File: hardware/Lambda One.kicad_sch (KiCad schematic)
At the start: 23 parts, among them IC1 DS1818, SW1 SW_Push, U8 74HC00, U9 74HC00, Y1 TFT680

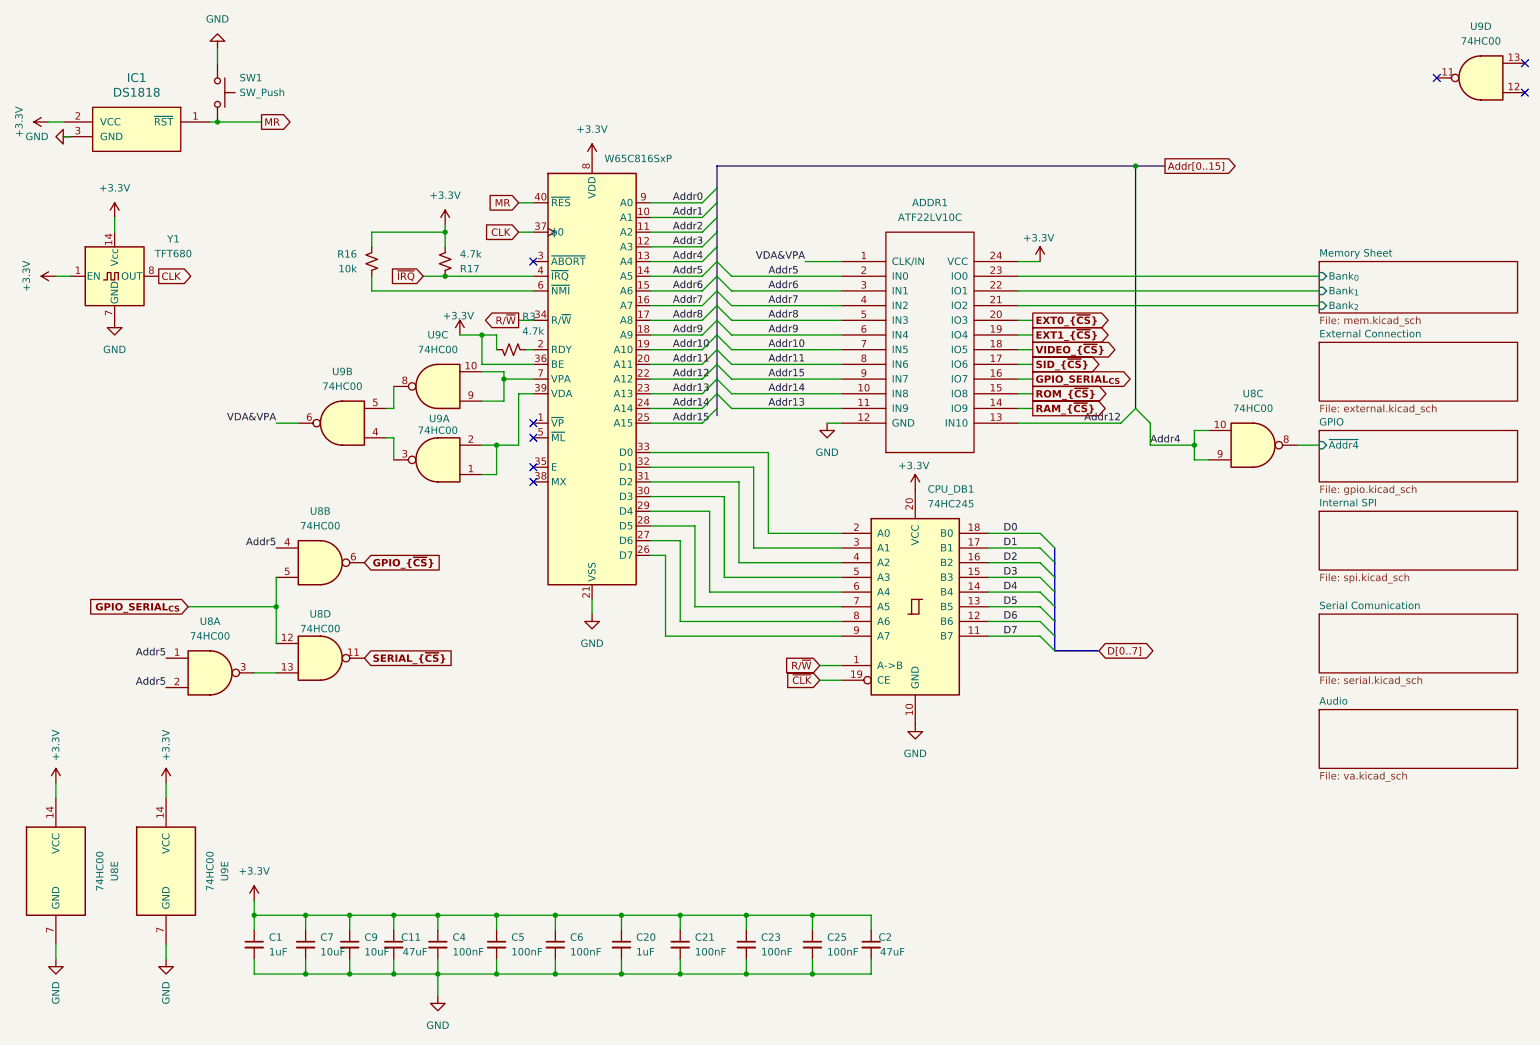
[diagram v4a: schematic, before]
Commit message: Removed old VPU
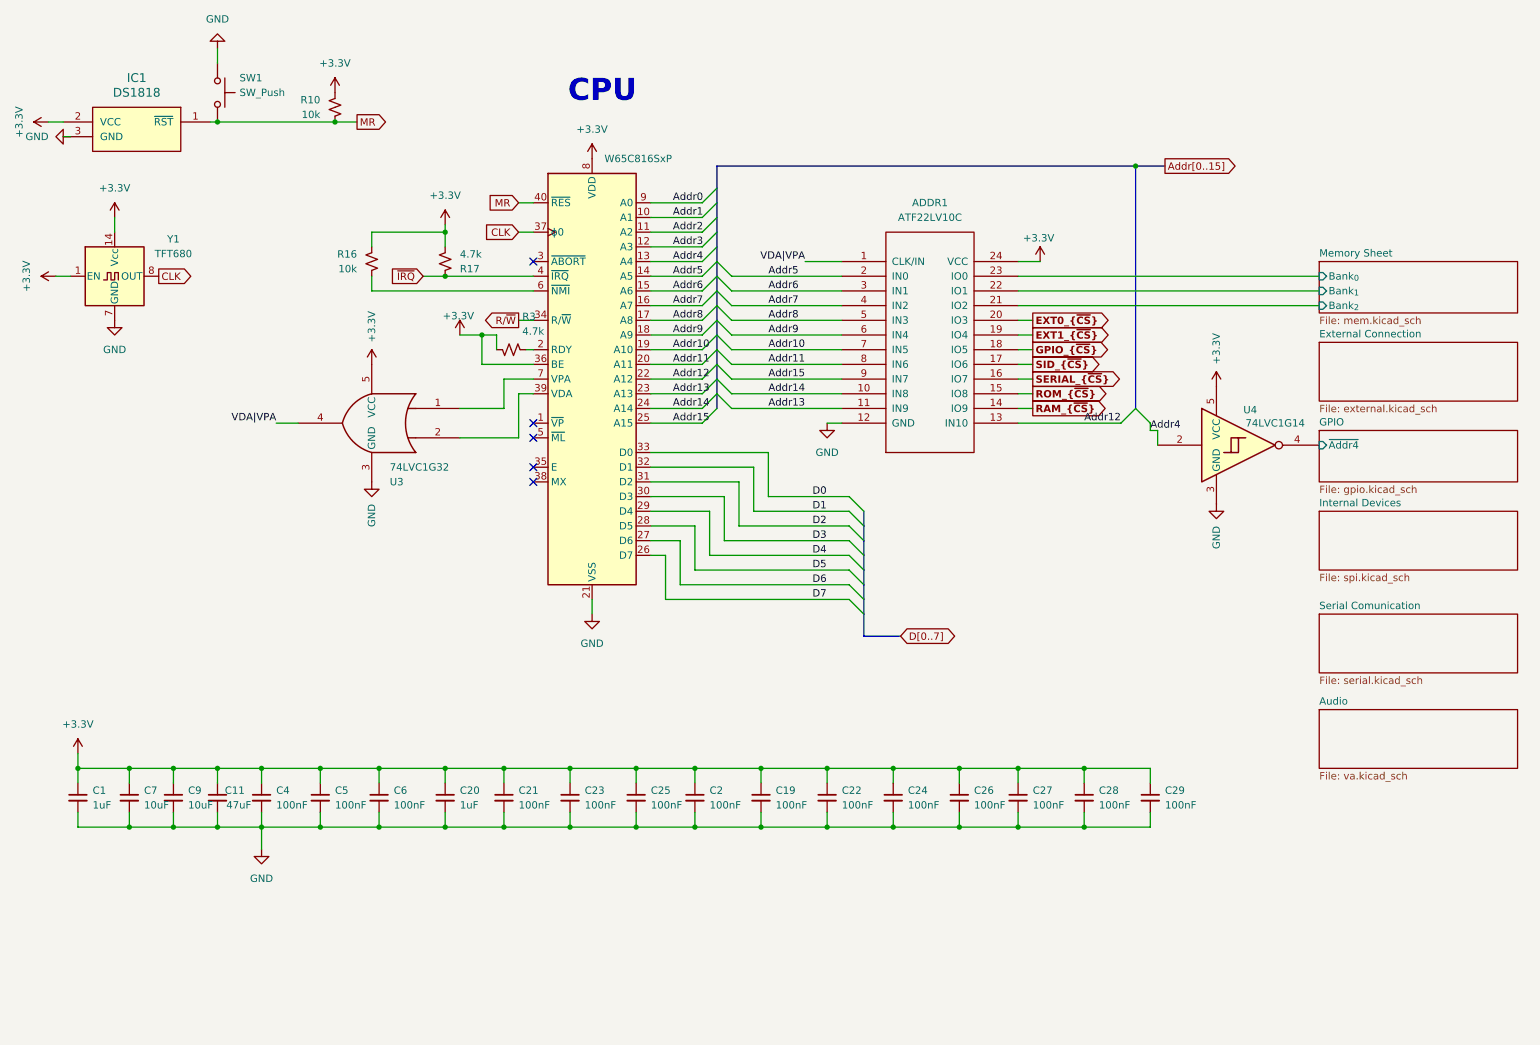
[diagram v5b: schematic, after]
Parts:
- removed CPU_DB1: 74HC245, Package_DIP:DIP-20_W7.62mm, symbol 74xx:74HC245
- removed U8, U9: 74HC00, Package_DIP:DIP-14_W7.62mm, symbol 74xx:74HC00
- added C19, C22, C24, C26, C27, C28, C29: 100nF, Capacitor_SMD:C_0603_1608Metric, symbol Device:C_Small
- added R10: 10k, Resistor_SMD:R_0603_1608Metric, symbol Device:R_Small_US
- added U3: 74LVC1G32, symbol 74xGxx:74LVC1G32
- added U4: 74LVC1G14, Package_TO_SOT_SMD:SOT-23-5, symbol 74xGxx:74LVC1G14
- C2: value 47uF -> 100nF; PartNumber CL10A105KB8NNNC -> CL10B104KB8NNNC
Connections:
- net GPIO_SERIAL_{CS} is gone; now on net SERIAL_{~{CS}}: ADDR1.16 (IO7)
- net VIDEO_{~{CS}} is gone; now on net GPIO_{~{CS}}: ADDR1.18 (IO5)
- net +3.3V: now also C19.1, C22.1, C24.1, C26.1, C27.1, C28.1, C29.1, R10.1, U3.5 (VCC), U4.5 (VCC)
- net Addr4: now also U4.2
- net D0: now also CPU1.33 (D0)
- net D1: now also CPU1.32 (D1)
- net D2: now also CPU1.31 (D2)
- net D3: now also CPU1.30 (D3)
- net D4: now also CPU1.29 (D4)
- net D5: now also CPU1.28 (D5)
- net D6: now also CPU1.27 (D6)
- net D7: now also CPU1.26 (D7)
- net GND: now also C19.2, C22.2, C24.2, C26.2, C27.2, C28.2, C29.2, U3.3 (GND), U4.3 (GND)
- net GPIO/~{Addr4}: now also U4.4
- net MR: now also R10.2
- net at CPU1.7 (VPA): now also U3.1
- net at CPU1.39 (VDA): now also U3.2
- net VDA&VPA renamed VDA|VPA
- net VDA|VPA: now also U3.4
- no-connect marks 8 -> 5
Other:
- sheet Internal SPI renamed Internal Devices
- note added: "CPU"
- moved on the sheet: C1, C11, C20, C21, C23, C25, C4, C5, C6, C7, C9

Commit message: Minor changes
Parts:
- U3: footprint (none) -> Package_TO_SOT_SMD:SOT-23-5
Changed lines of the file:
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@@
 			)
 		)
-		(property "Footprint" ""
+		(property "Footprint" "Package_TO_SOT_SMD:SOT-23-5"
 			(at 77.47 88.9 0)
 			(effects
